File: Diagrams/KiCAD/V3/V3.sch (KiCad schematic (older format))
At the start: 26 parts, among them M1 Stepper_Motor_bipolar, M2 Stepper_Motor_bipolar, M3 Stepper_Motor_bipolar, U1 TSOP38238, U2 NodeMCU_1.0_(ESP-12E), U3 74HC595, U4 74HC595

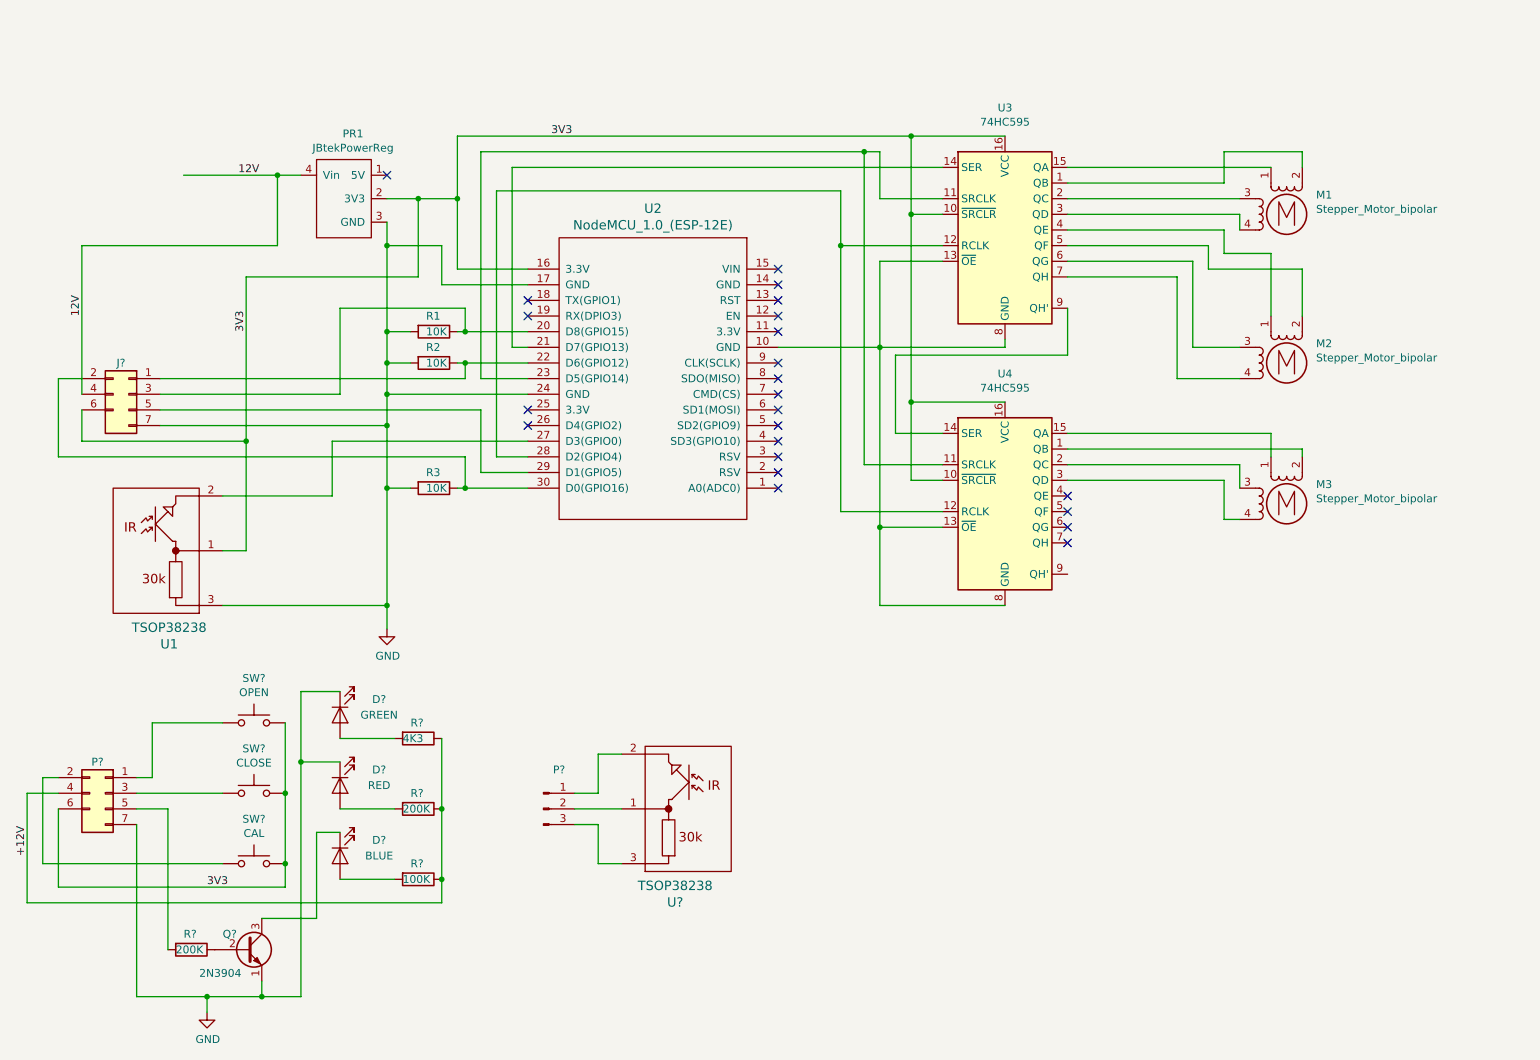
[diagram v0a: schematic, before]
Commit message: More work on KiCAD schematic.
Created and added driver board for 28BYJ stepper (board: SBT0811)

Added more connectors. Next: finish up connectors to driver boards.
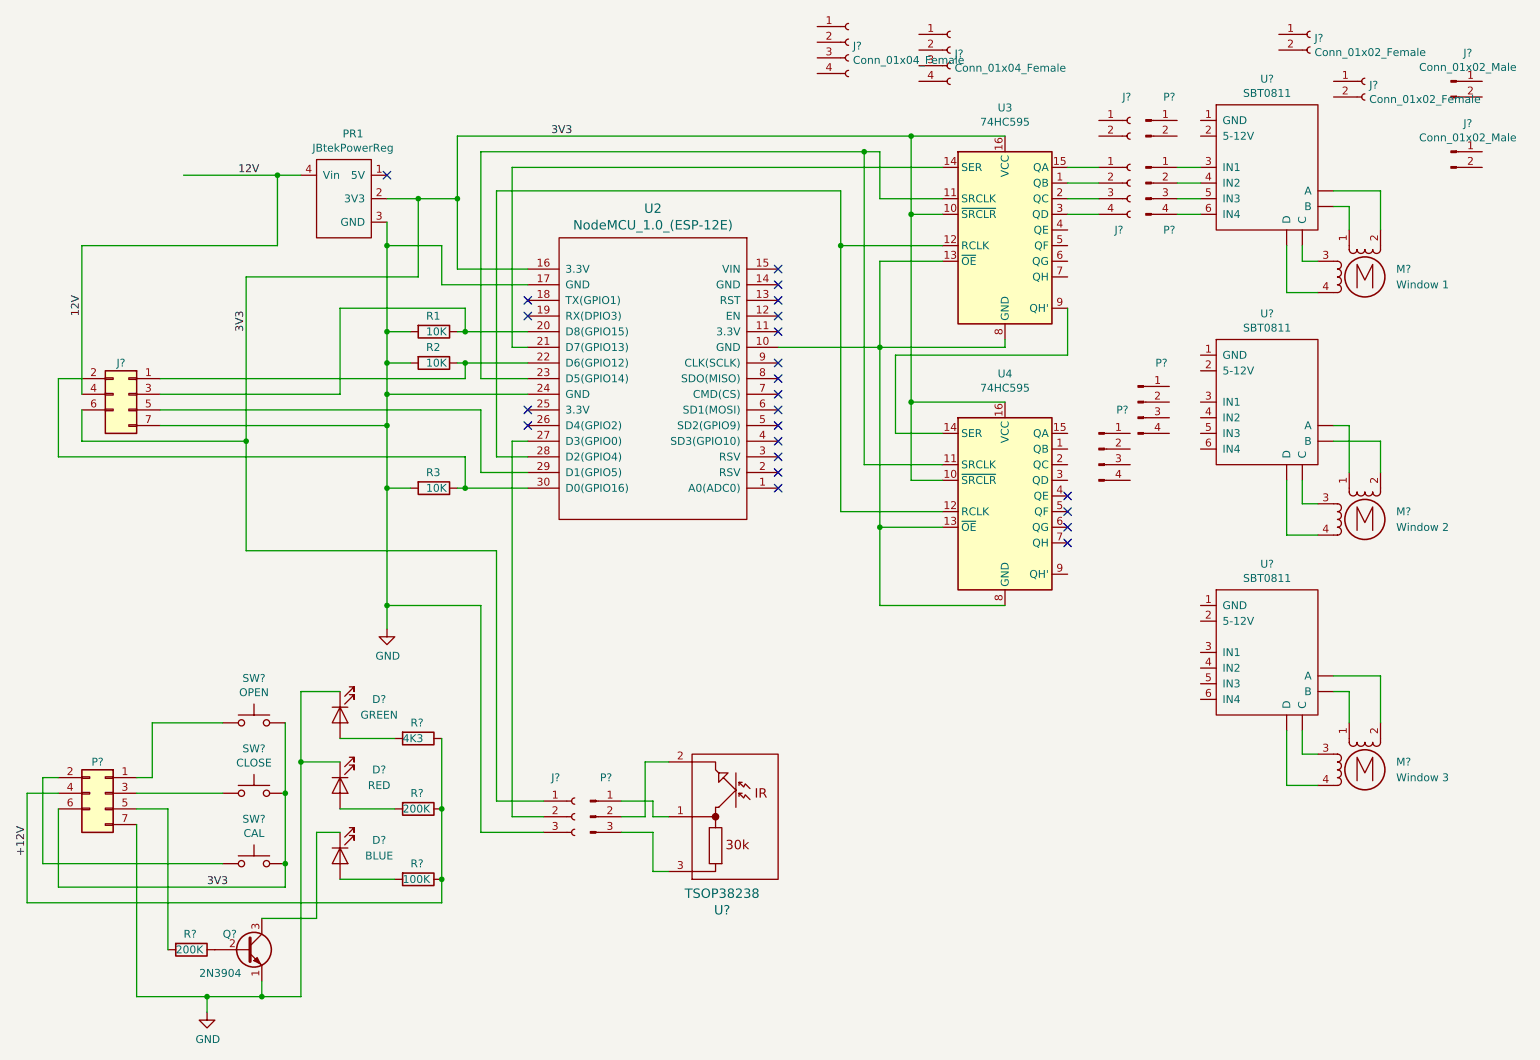
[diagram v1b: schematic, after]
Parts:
- removed M1, M2, M3: Stepper_Motor_bipolar, symbol Motor:Stepper_Motor_bipolar
- removed U1: TSOP38238, symbol Kip_Custom_Lib:TSOP38238
- added J?: (no value), symbol Connector:Conn_01x03_Female
- added J?: (no value), symbol Connector:Conn_01x04_Female
- added J? (x2): Conn_01x04_Female, symbol Connector:Conn_01x04_Female
- added J? (x2): Conn_01x02_Male, symbol Connector:Conn_01x02_Male
- added J? (x2): Conn_01x02_Female, symbol Connector:Conn_01x02_Female
- added J?: (no value), symbol Connector:Conn_01x02_Female
- added M?: Window 1, symbol Motor:Stepper_Motor_bipolar
- added M?: Window 2, symbol Motor:Stepper_Motor_bipolar
- added M?: Window 3, symbol Motor:Stepper_Motor_bipolar
- added P? (x3): (no value), symbol Connector:Conn_01x04_Male
- added P?: (no value), symbol Connector:Conn_01x02_Male
- added U? (x3): SBT0811, symbol ProjectCustom:SBT0811
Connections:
- net 3V3: now also J?.1 (Pin_1)
- net GND: now also J?.3 (Pin_3)
- net at U3.15 (QA): now also J?.1 (Pin_1)
- net at U3.1 (QB): now also J?.2 (Pin_2)
- net at U3.2 (QC): now also J?.3 (Pin_3)
- net at U3.3 (QD): now also J?.4 (Pin_4)
- net at U2.27 (D3(GPIO0)): now also J?.2 (Pin_2)
- net at U?.1: now also P?.1 (Pin_1); no longer P?.2 (Pin_2)
- net at U?.2: now also P?.2 (Pin_2); no longer P?.1 (Pin_1)
- new net: M?.1, U?.~ (D) (x3)
- new net: M?.2 (-), U?.~ (D) (x3)
- new net: M?.3, U?.~ (D) (x3)
- new net: M?.4, U?.~ (D) (x3)
- new net: P?.1 (Pin_1), U?.3 (IN1)
- new net: P?.2 (Pin_2), U?.4 (IN2)
- new net: P?.3 (Pin_3), U?.5 (IN3)
- new net: P?.4 (Pin_4), U?.6 (IN4)
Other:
- moved on the sheet: P?, U?

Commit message: Finished V3 KiCAD schematic.
Added colors for stepper connections to ensure correct rotation!
Colors obtained from breadboard pictures.
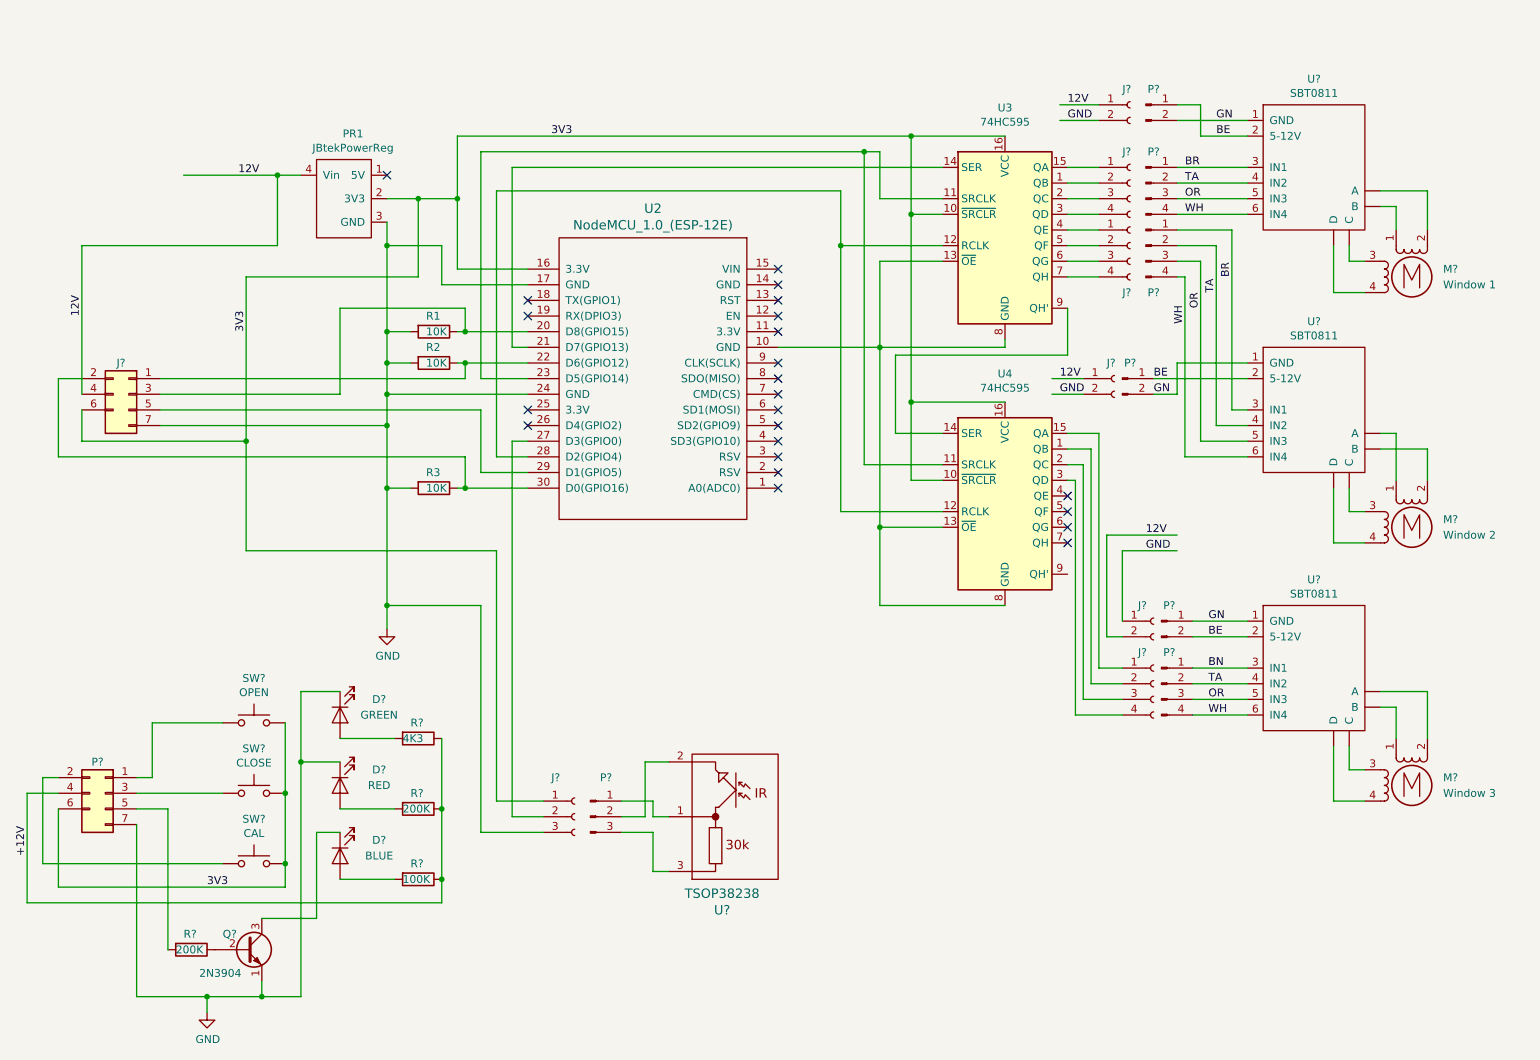
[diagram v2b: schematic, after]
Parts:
- removed J? (x2): Conn_01x04_Female, symbol Connector:Conn_01x04_Female
- removed J? (x2): Conn_01x02_Male, symbol Connector:Conn_01x02_Male
- removed J? (x2): Conn_01x02_Female, symbol Connector:Conn_01x02_Female
- removed P? (x2): (no value), symbol Connector:Conn_01x04_Male
- added J? (x2): (no value), symbol Connector:Conn_01x04_Female
- added J? (x2): (no value), symbol Connector:Conn_01x02_Female
- added P? (x2): (no value), symbol Connector:Conn_01x04_Male
- added P? (x2): (no value), symbol Connector:Conn_01x02_Male
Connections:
- net labels added: BE, BN, BR, GN, OR, TA, WH
- wire segments 176 -> 227
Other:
- moved on the sheet: J?, M?, P?, U?
